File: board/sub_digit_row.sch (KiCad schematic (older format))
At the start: 41 parts, among them Q601 Q_PMOS_GSD, Q602 Q_PMOS_GSD, Q603 Q_PMOS_GSD, Q604 Q_PMOS_GSD, Q605 Q_PMOS_GSD, Q606 Q_PMOS_GSD, Q607 Q_PMOS_GSD, Q608 Q_PMOS_GSD, U601 TPIC6D595, U602 TPIC6D595, U603 TPIC6D595

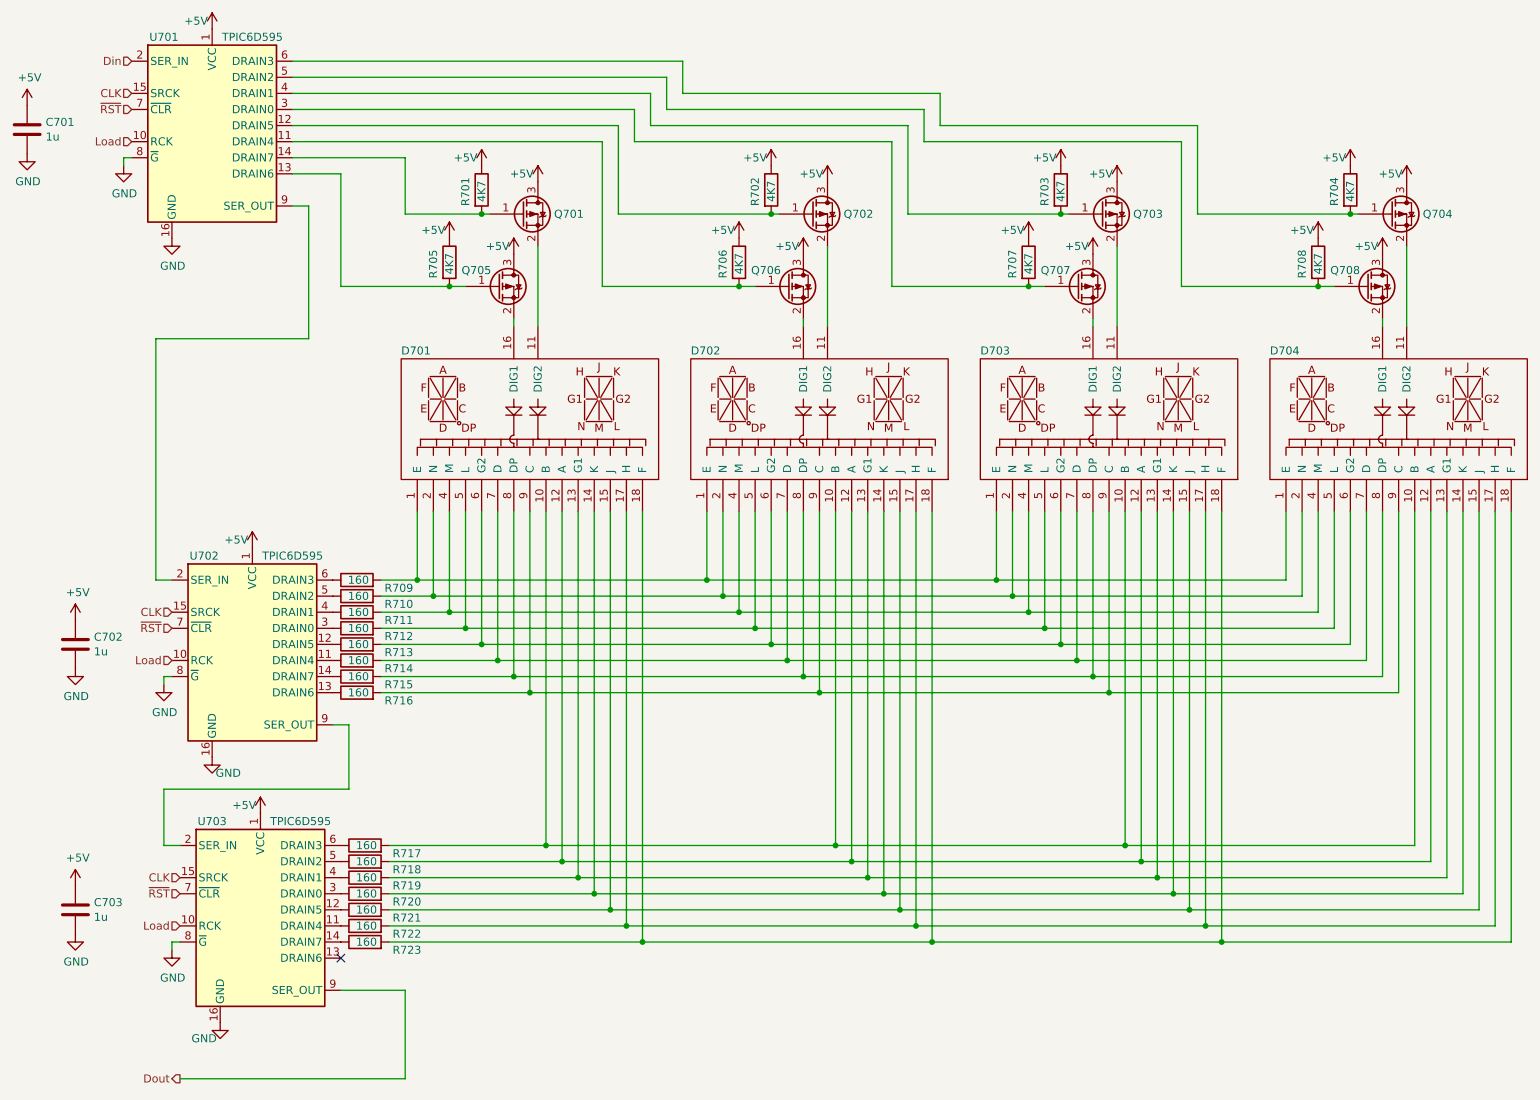
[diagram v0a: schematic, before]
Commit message: Most footprints associated
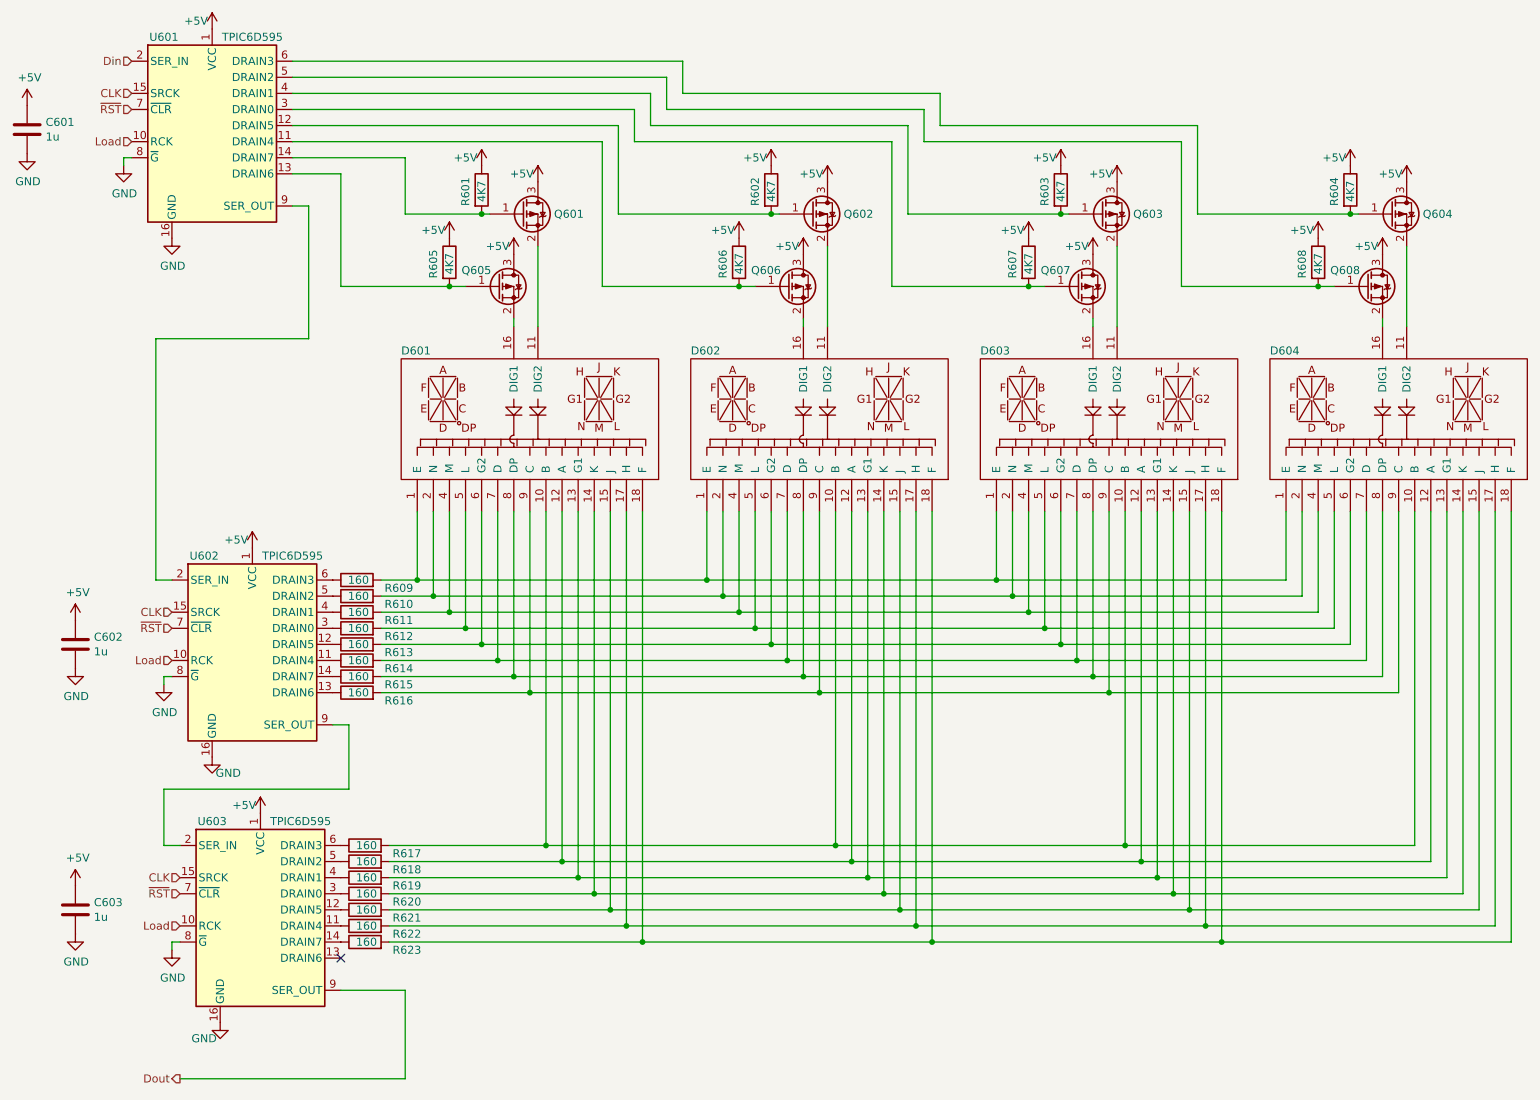
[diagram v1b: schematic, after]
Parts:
- C601, C602, C603: footprint (none) -> Capacitor_SMD:C_0603_1608Metric
- R601, R602, R603, R604, R605, R606, R607, R608: footprint (none) -> Resistor_SMD:R_0603_1608Metric

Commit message: Almost all footprints done
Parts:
- D601, D602, D603, D604: value (none) -> 14-segment; footprint (none) -> quokka:14-segment

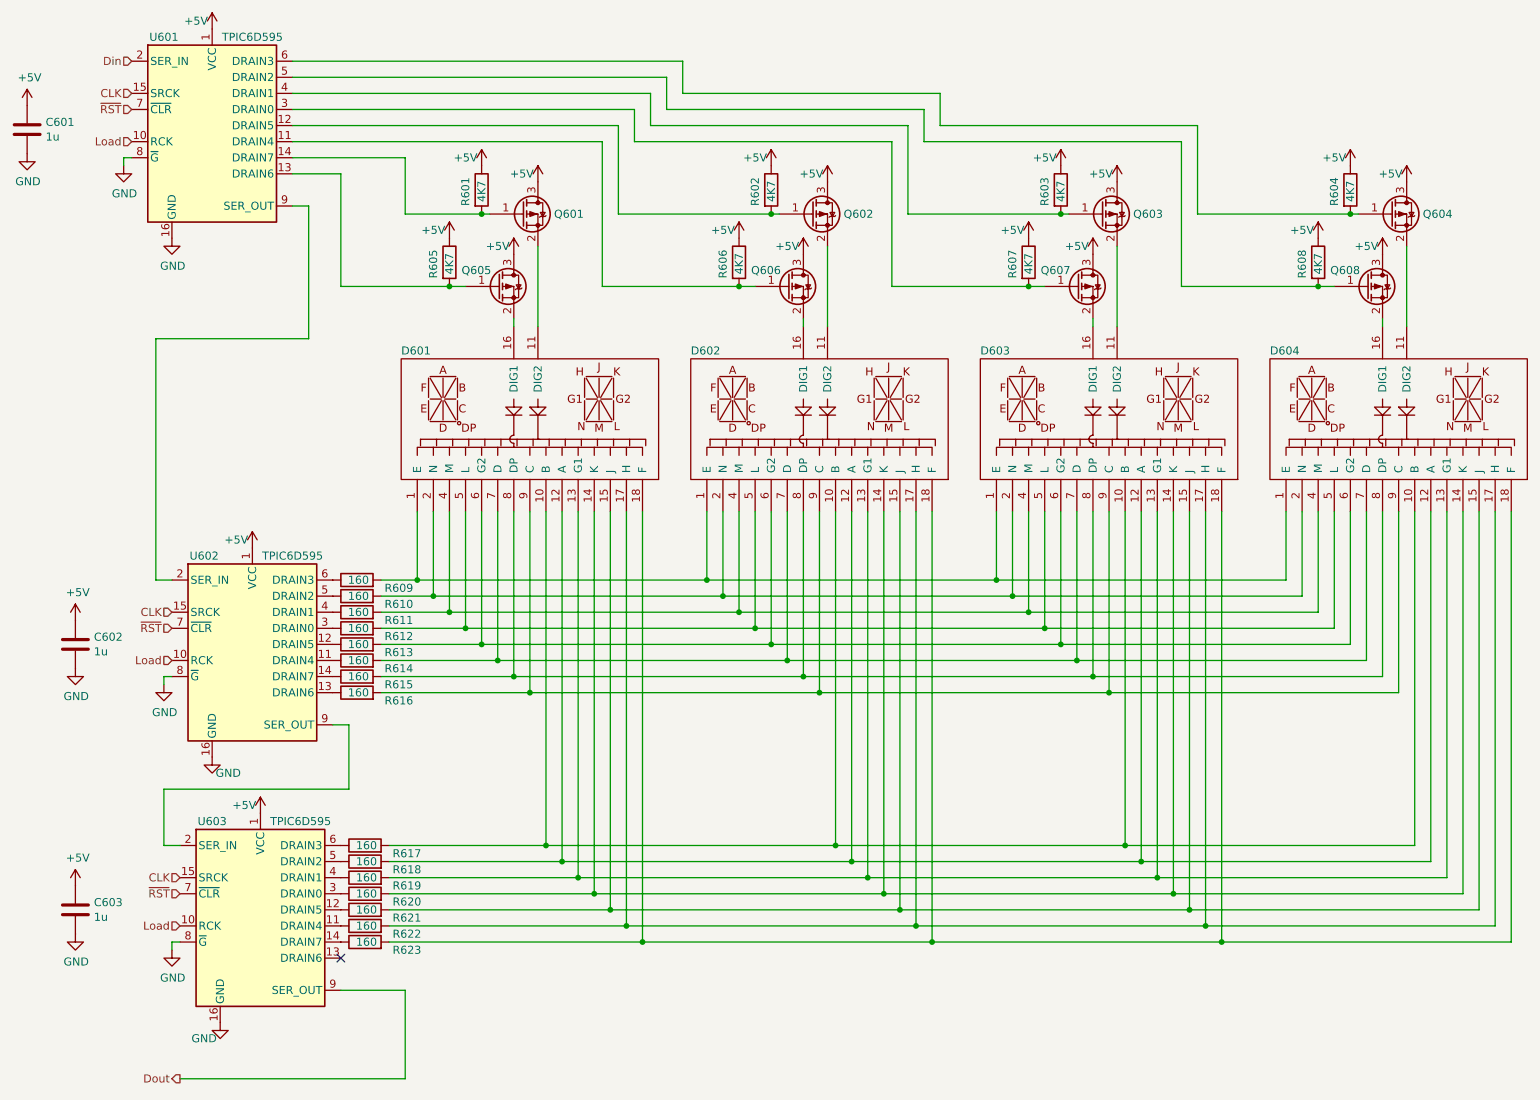
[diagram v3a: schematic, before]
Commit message: Power supply routed
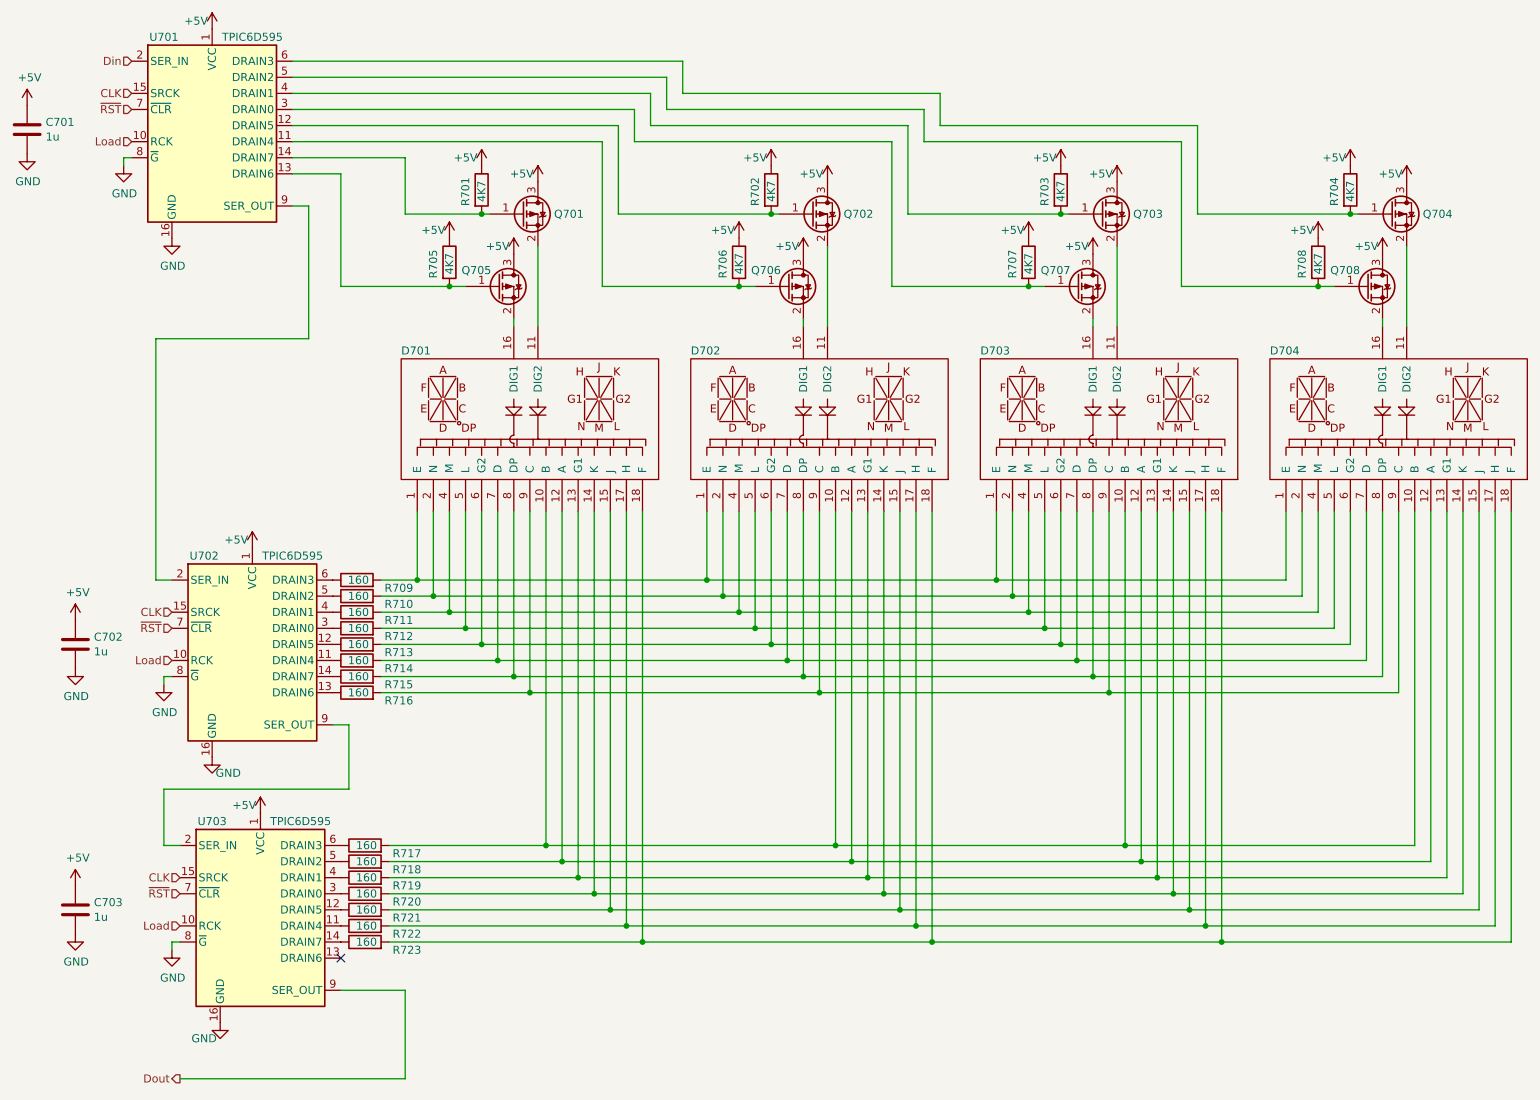
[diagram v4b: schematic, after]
